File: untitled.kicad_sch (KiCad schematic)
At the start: 5 parts, among them SW1 SW_MEC_5G

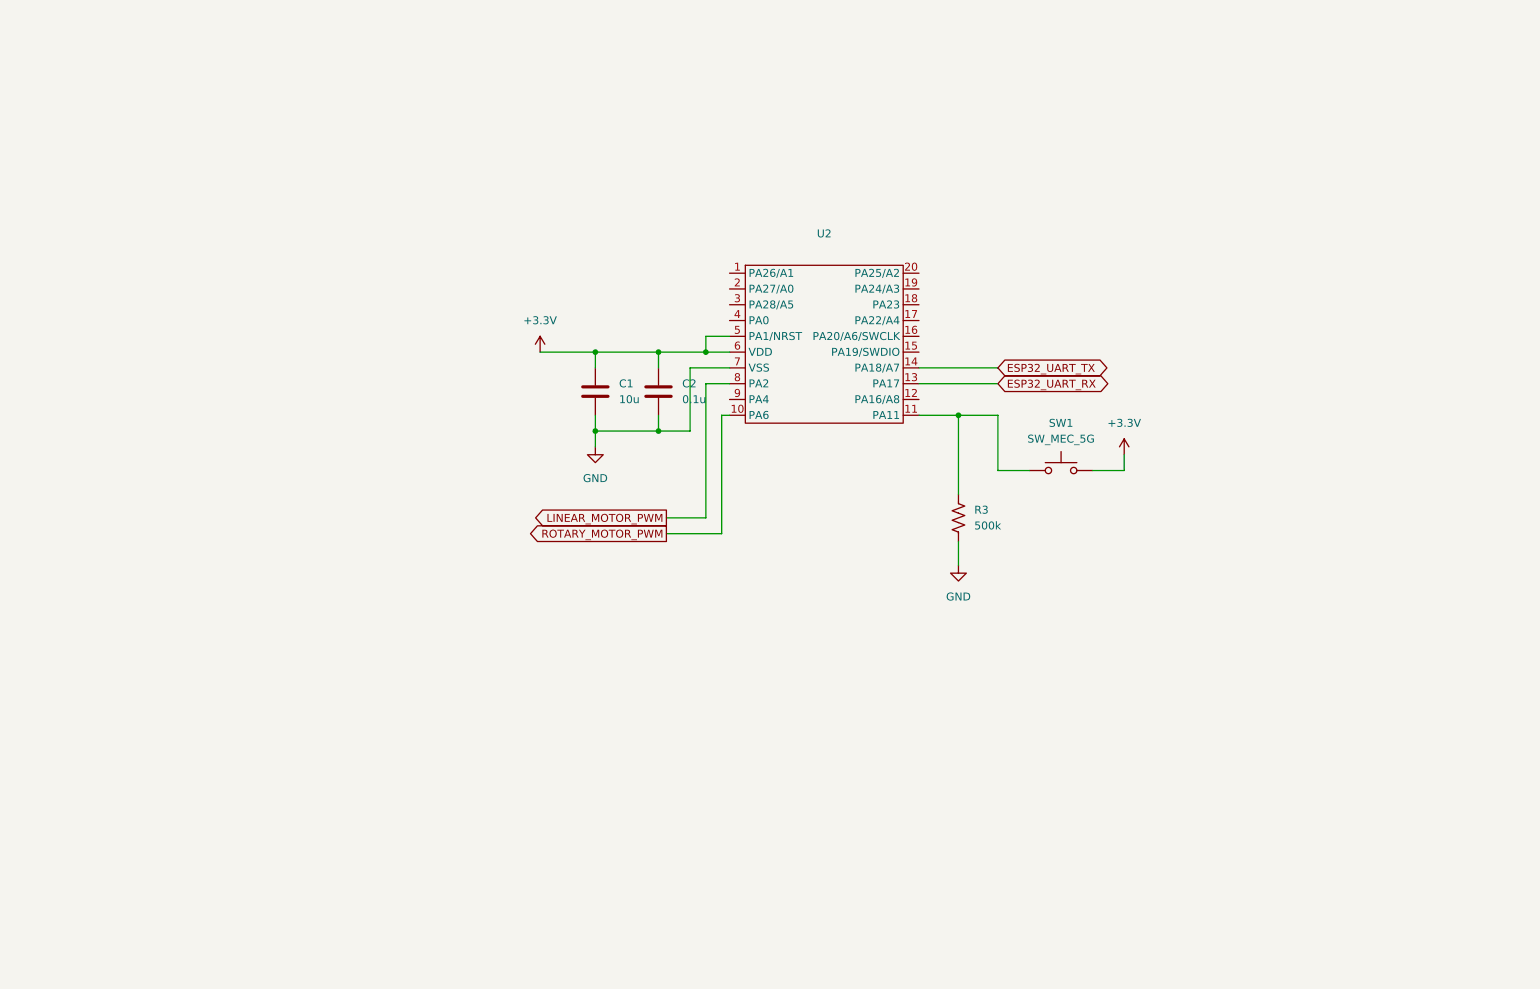
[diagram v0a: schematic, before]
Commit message: Fixed things, added microphone amplifier, ...
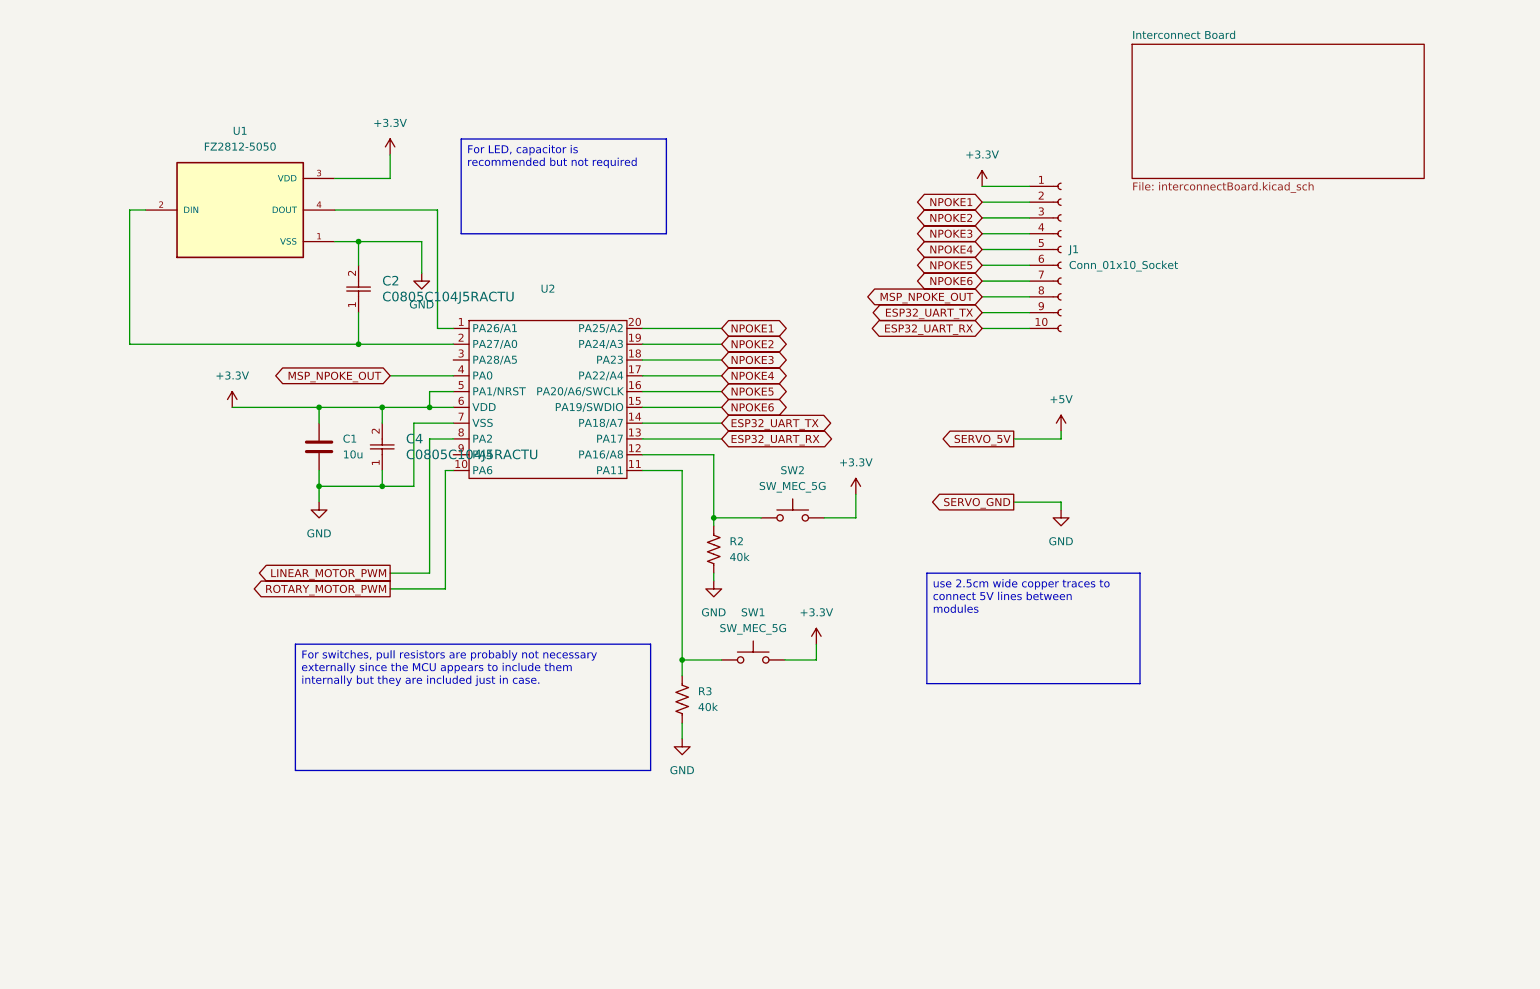
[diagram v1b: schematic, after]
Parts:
- removed C2: 0.1u, symbol Device:C
- added C2, C4: C0805C104J5RACTU, CAPC220145_88N_KEM, symbol roseActuatorLibrary:C0805C104J5RACTU
- added J1: Conn_01x10_Socket, symbol Connector:Conn_01x10_Socket
- added R2: 40k, symbol Device:R_US
- added SW2: SW_MEC_5G, symbol Switch:SW_MEC_5G
- added U1: FZ2812-5050, FZ2812-5050:LED_FZ2812-5050, symbol roseActuatorLibrary:FZ2812-5050
- R3: value 500k -> 40k
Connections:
- net +3.3V: now also C4.2, J1.1 (Pin_1), SW2.3 (B), SW2.4 (B), U1.3 (VDD)
- net ESP32_UART_RX: now also J1.10 (Pin_10)
- net ESP32_UART_TX: now also J1.9 (Pin_9)
- net GND: now also C2.2, C4.1, R2.2, U1.1 (VSS)
- net at U2.1 (PA26/A1): now also U1.4 (DOUT)
- net at U2.12 (PA16/A8): now also R2.1, SW2.1 (A), SW2.2 (A)
- net NPOKE6: now reaches U2.15 (PA19/SWDIO)
- net NPOKE6: now also J1.7 (Pin_7)
- net NPOKE5: now reaches U2.16 (PA20/A6/SWCLK)
- net NPOKE5: now also J1.6 (Pin_6)
- net NPOKE4: now reaches U2.17 (PA22/A4)
- net NPOKE4: now also J1.5 (Pin_5)
- net NPOKE3: now reaches U2.18 (PA23)
- net NPOKE3: now also J1.4 (Pin_4)
- net NPOKE2: now reaches U2.19 (PA24/A3)
- net NPOKE2: now also J1.3 (Pin_3)
- net at U2.2 (PA27/A0): now also C2.1, U1.2 (DIN)
- net NPOKE1: now reaches U2.20 (PA25/A2)
- net NPOKE1: now also J1.2 (Pin_2)
- net MSP_NPOKE_OUT: now reaches U2.4 (PA0)
- net MSP_NPOKE_OUT: now also J1.8 (Pin_8)
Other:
- added sheet Interconnect Board (interconnectBoard.kicad_sch)
- moved on the sheet: C1, R3, SW1, U2

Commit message: Added footprint for MSPM0C1103SDGS20R
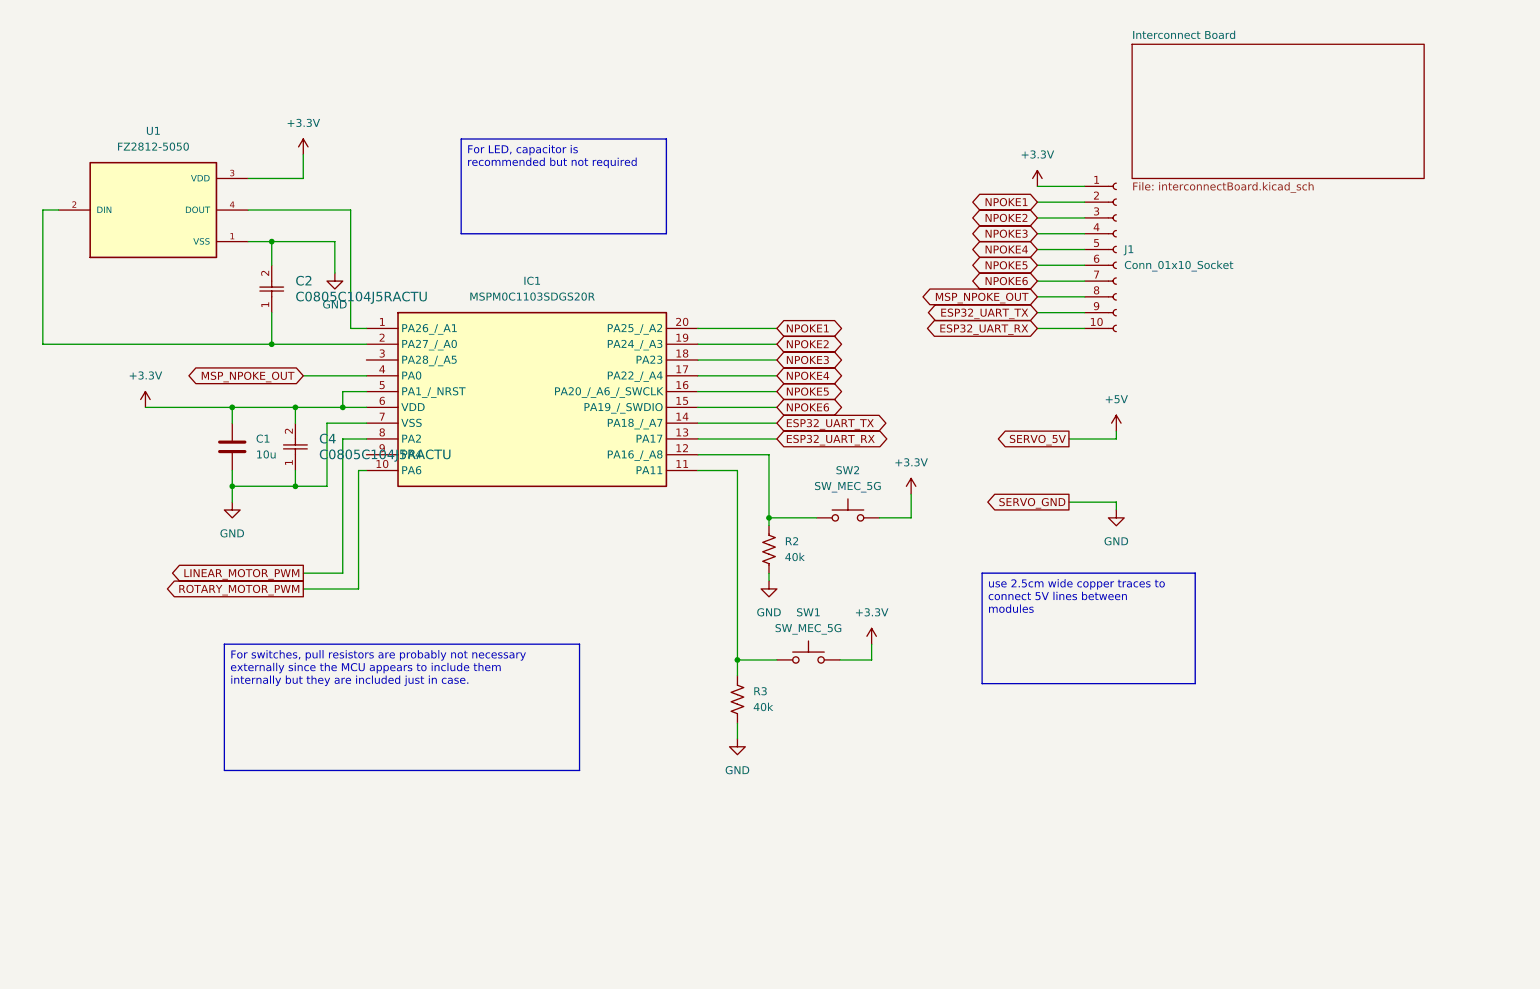
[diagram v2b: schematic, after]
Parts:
- removed U2: ~, symbol roseActuatorLibrary:MSPM0C1103SDGS20R
- added IC1: MSPM0C1103SDGS20R, SOP50P490X110-20N, symbol MSPM0C1103SDGS20R:MSPM0C1103SDGS20R
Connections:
- net +3.3V: now also IC1.5 (PA1_/_NRST), IC1.6 (VDD)
- net ESP32_UART_RX: now also IC1.13 (PA17)
- net ESP32_UART_TX: now also IC1.14 (PA18_/_A7)
- net GND: now also IC1.7 (VSS)
- net LINEAR_MOTOR_PWM: now also IC1.8 (PA2)
- net MSP_NPOKE_OUT: now also IC1.4 (PA0)
- net NPOKE1: now also IC1.20 (PA25_/_A2)
- net NPOKE2: now also IC1.19 (PA24_/_A3)
- net NPOKE3: now also IC1.18 (PA23)
- net NPOKE4: now also IC1.17 (PA22_/_A4)
- net NPOKE5: now also IC1.16 (PA20_/_A6_/_SWCLK)
- net NPOKE6: now also IC1.15 (PA19_/_SWDIO)
- net ROTARY_MOTOR_PWM: now also IC1.10 (PA6)
- net at C2.1, U1.2 (DIN): now also IC1.2 (PA27_/_A0)
- net at U1.4 (DOUT): now also IC1.1 (PA26_/_A1)
- net at R3.1, SW1.1 (A), SW1.2 (A): now also IC1.11 (PA11)
- net at R2.1, SW2.1 (A), SW2.2 (A): now also IC1.12 (PA16_/_A8)
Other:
- moved on the sheet: C1, C2, C4, J1, R2, R3, SW1, SW2, U1

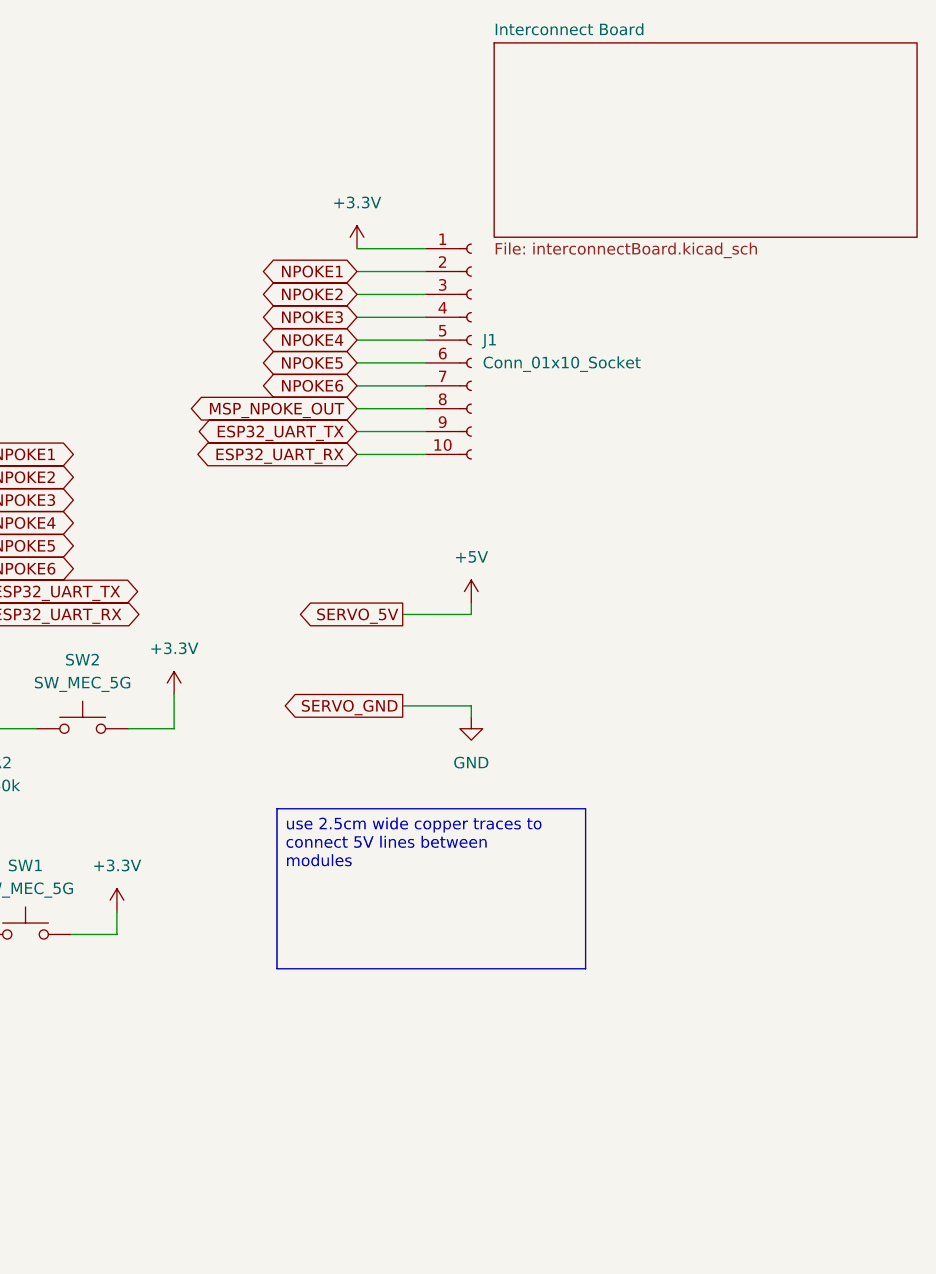
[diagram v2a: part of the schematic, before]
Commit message: Fixed amplifier resistors, fixed potentiometer
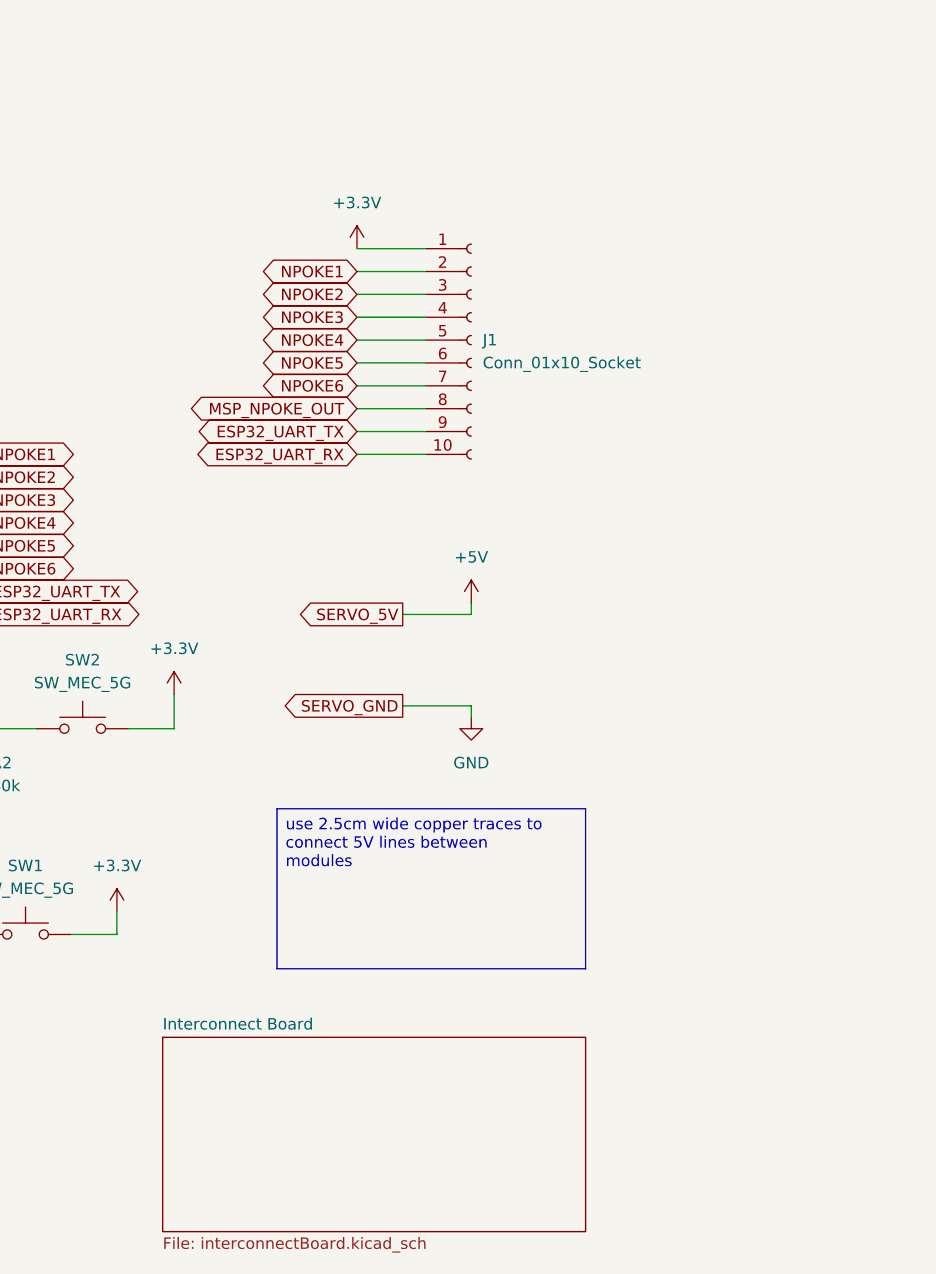
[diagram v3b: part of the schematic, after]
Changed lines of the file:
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@@
 	)
 	(sheet
-		(at 193.04 21.59)
+		(at 156.21 132.08)
 		(size 46.99 21.59)
 		(exclude_from_sim no)
@@
 		)
 		(property "Sheetname" "Interconnect Board"
-			(at 193.04 20.8784 0)
+			(at 156.21 131.3684 0)
 			(effects
 				(font
@@
 		)
 		(property "Sheetfile" "interconnectBoard.kicad_sch"
-			(at 193.04 43.7646 0)
+			(at 156.21 154.2546 0)
 			(effects
 				(font
